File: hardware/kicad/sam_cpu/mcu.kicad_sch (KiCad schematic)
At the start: 38 parts, among them J19 USB-C (to Pi), J20 SWD, SW1 RESET, SW2 BOOTSEL, U4 RP2354B, U5 TPS3808G33, Y1 12MHz

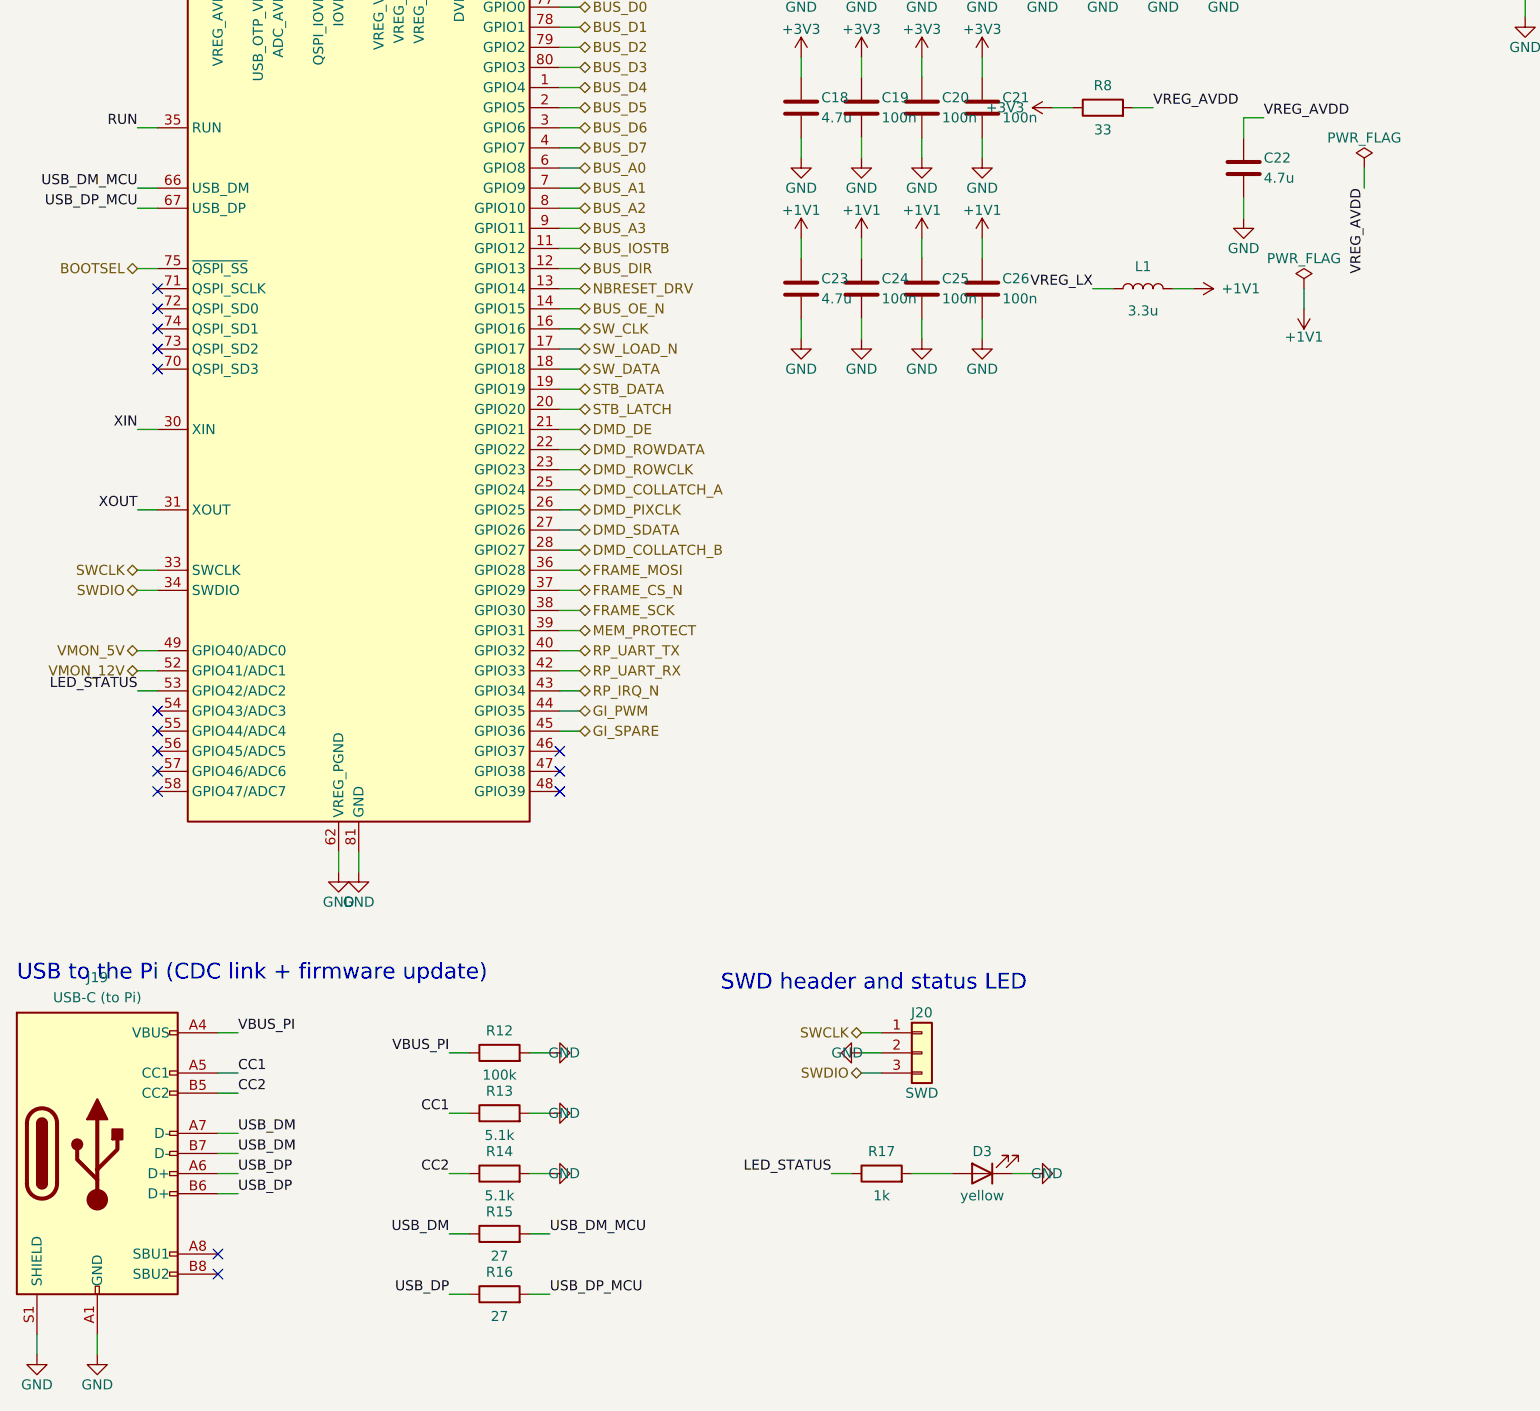
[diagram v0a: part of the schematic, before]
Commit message: Move the schematic to KiCad 10
Sheets regenerated from the KiCad 10.0.5 symbol library and saved in the
KiCad 10 file format with kicad-cli 10.0.6. ERC: 0 errors, 1 warning;
netlist unchanged (1266 pins, 299 nets).

Co-Authored-By: Claude Opus 5.5 (1M context) <noreply@anthropic.com>
Claude-Session: https://claude.ai/code/session_019DLTv1F2PjepjxqiUcAMKV
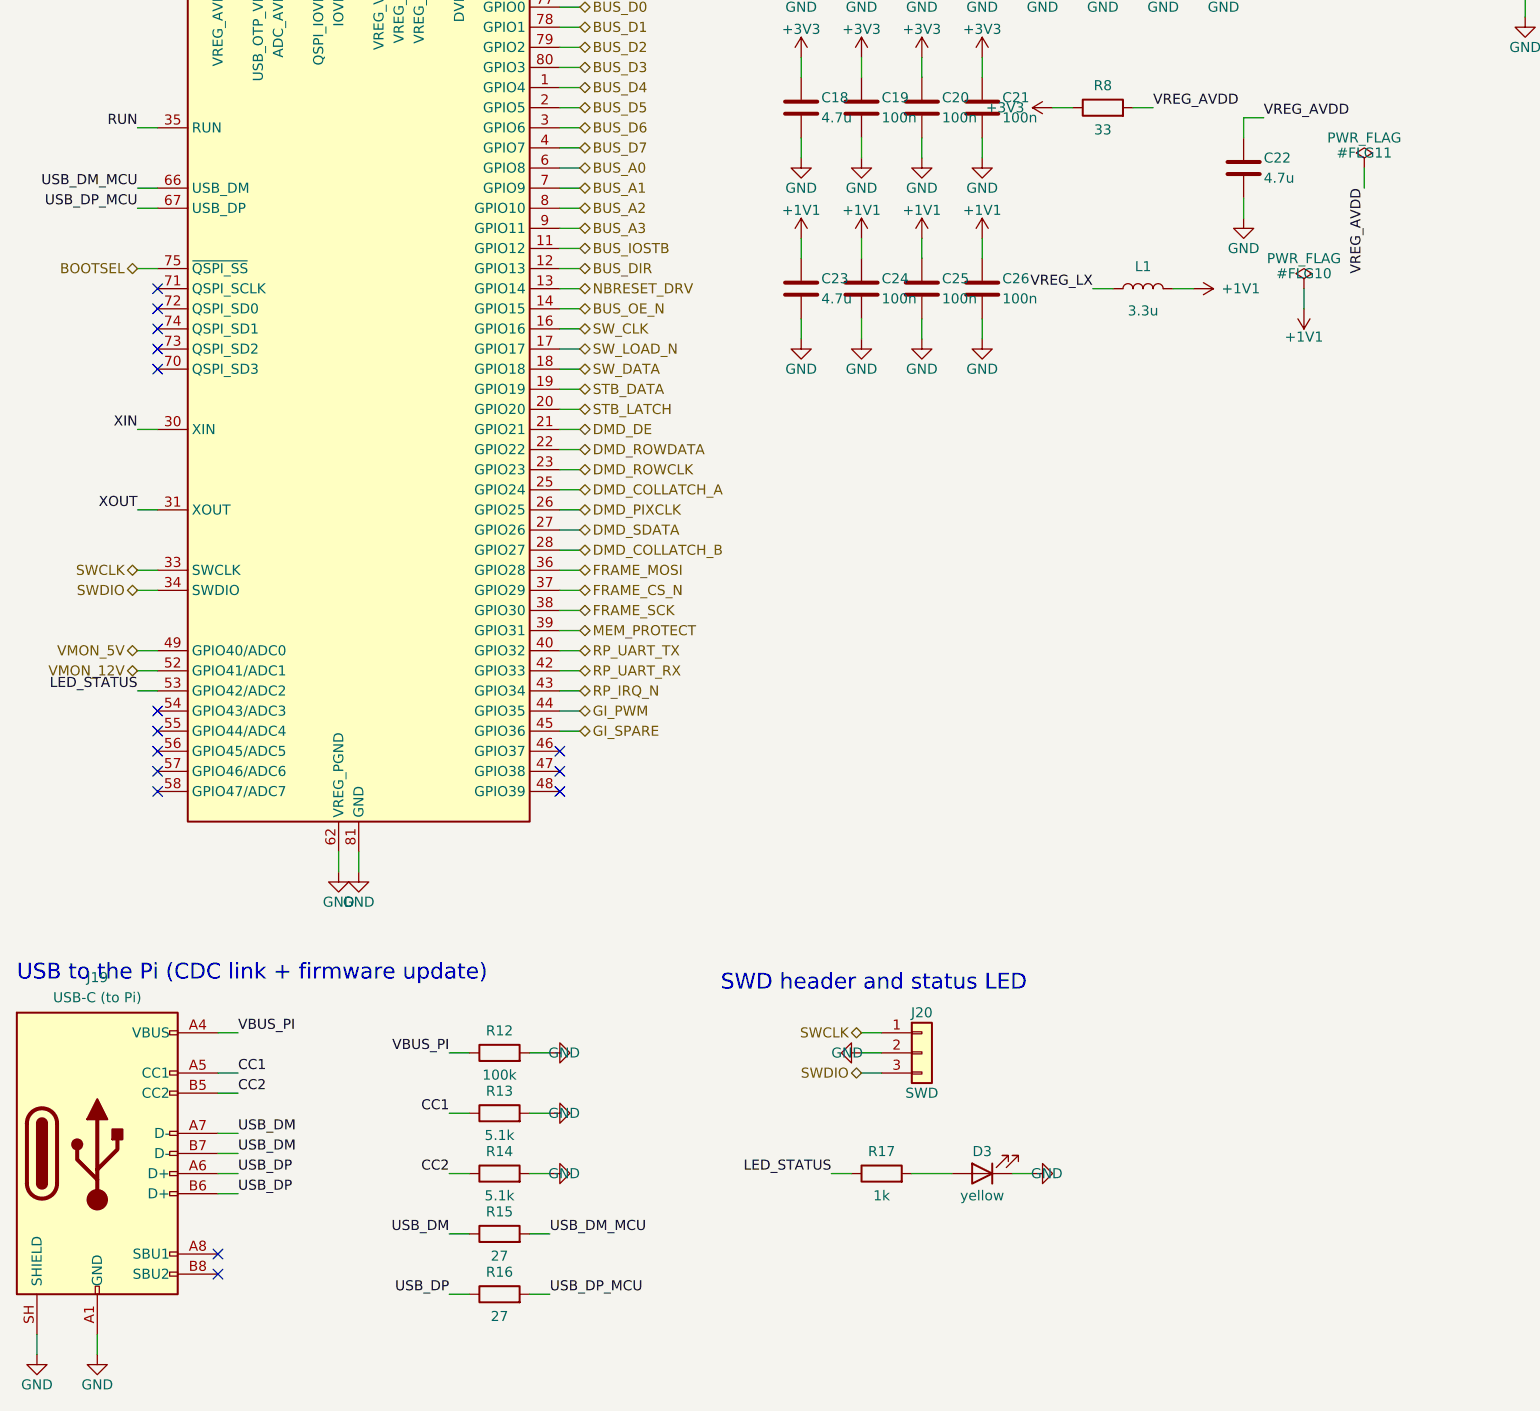
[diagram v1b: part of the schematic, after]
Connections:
- net GND: now also J19.SH (SHIELD); no longer J19.S1 (SHIELD)

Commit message: Redraw the schematic with wires (draft 0.2)
Every connection is now a wire, and each connector sits on the page of the
parts that drive or read it (Pi header with the RP2354B, J6/J12 with their
comparators and 74HC165, J1 with the 74HC595, J2/J3/J13 with their filters).
Signals between pages use global labels with page references. The Pi page is
merged into the MCU page; the Pi 4 sits on the 40-pin header J21.

ERC: 0 errors, 1 warning. Netlist check: 1266 pins, 299 nets, no differences.

Co-Authored-By: Claude Opus 5.5 (1M context) <noreply@anthropic.com>
Claude-Session: https://claude.ai/code/session_019DLTv1F2PjepjxqiUcAMKV
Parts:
- removed C10: 100n, Capacitor_SMD:C_0603_1608Metric, symbol Device:C
- added C29: 15p, Capacitor_SMD:C_0603_1608Metric, symbol Device:C
- added J21: Raspberry Pi 40-pin, Connector_PinSocket_2.54mm:PinSocket_2x20_P2.54mm_Vertical, symbol Connector:Raspberry_Pi_2_3
- added R18, R19: 33, Resistor_SMD:R_0603_1608Metric, symbol Device:R
- added R20, R21: 1k, Resistor_SMD:R_0603_1608Metric, symbol Device:R
- added R22: 10k, Resistor_SMD:R_0603_1608Metric, symbol Device:R
- C11, C12, C24: value 100n -> 4.7u; footprint Capacitor_SMD:C_0603_1608Metric -> Capacitor_SMD:C_0805_2012Metric
- C18, C22, C23: value 4.7u -> 100n; footprint Capacitor_SMD:C_0805_2012Metric -> Capacitor_SMD:C_0603_1608Metric
- C27: value 15p -> 100n
- R10: value 10k -> 100k
- R11: value 1k -> 5.1k
- R12: value 100k -> 5.1k
- R13, R14: value 5.1k -> 27
- R15, R16: value 27 -> 1k
- R9: value 1k -> 10k
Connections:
- net +1V1: now also C27.1; no longer C23.1
- net +3V3: now also C22.1, C23.1, R9.1, R22.1; no longer C11.1, R10.2
- net BOOTSEL: now also R15.2, R21.2; no longer R11.1
- net GND: now also R10.2, R11.2, C29.2, J21.14 (GND), J21.20 (GND), J21.25 (GND), J21.30 (GND), J21.34 (GND), J21.39 (GND), J21.6 (GND), J21.9 (GND); no longer R13.2, R14.2
- net MR_N: now also R20.2
- net SWCLK: now also J21.18 (GPIO24)
- net SWDIO: now also J21.22 (GPIO25)
- net at D3.2 (A): now also R17.1; no longer R17.2
- net BOOTSEL_BTN: no longer names the net of SW2.1
- net BOOTSEL_BTN: now also R15.1; no longer R11.2
- net CC1: no longer names the net of J19.A5 (CC1)
- net CC1: now also R11.1; no longer R13.1
- net CC2: no longer names the net of J19.B5 (CC2)
- net CC2: now also R12.1; no longer R14.1
- net FRAME_CS_N: no longer names the net of U4.37 (GPIO29)
- net FRAME_CS_N: now also J21.24 (~{CE0}/GPIO8)
- net FRAME_MOSI: no longer names the net of U4.36 (GPIO28)
- net FRAME_MOSI: now also J21.19 (MOSI0/GPIO10)
- net FRAME_SCK: no longer names the net of U4.38 (GPIO30)
- net FRAME_SCK: now also J21.23 (SCLK0/GPIO11)
- net LED_STATUS: no longer names the net of U4.53 (GPIO42/ADC2)
- net LED_STATUS: now also R17.2; no longer R17.1
- net RP_IRQ_N: no longer names the net of U4.43 (GPIO34)
- net RP_IRQ_N: now also J21.16 (GPIO23), R22.2
- net RP_UART_RX: no longer names the net of U4.42 (GPIO33)
- net RP_UART_RX: now also R18.2
- net RP_UART_TX: no longer names the net of U4.40 (GPIO32)
- net RP_UART_TX: now also R19.2
- net RUN: no longer names the net of U4.35 (RUN), U5.1 (~{RESET})
- net RUN: now also R9.2; no longer R10.1
- net USB_DM: no longer names the net of J19.A7 (D-), J19.B7 (D-)
- net USB_DM: now also R13.1; no longer R15.1
- net USB_DM_MCU: no longer names the net of U4.66 (USB_DM)
- net USB_DM_MCU: now also R13.2; no longer R15.2
- net USB_DP: no longer names the net of J19.A6 (D+), J19.B6 (D+)
- net USB_DP: now also R14.1; no longer R16.1
- net USB_DP_MCU: no longer names the net of R16.2
- net USB_DP_MCU: now also U4.31 (XOUT); no longer U4.67 (USB_DP)
- net VBUS_PI: no longer names the net of J19.A4 (VBUS), J19.A9 (VBUS), J19.B4 (VBUS), J19.B9 (VBUS)
- net VBUS_PI: now also R10.1; no longer R12.1
- net VREG_AVDD: no longer names the net of R8.2, U4.61 (VREG_AVDD)
- net VREG_AVDD: now also C11.1; no longer C22.1
- net VREG_LX: no longer names the net of L1.1, U4.63 (VREG_LX)
- net XIN: no longer names the net of U4.30 (XIN), Y1.1
- net XIN: now also C28.1; no longer C27.1
- removed net XOUT: R9.1, U4.31 (XOUT)
- removed net XTAL_OUT: C28.1, R9.2, Y1.3
- new net: J21.13 (GPIO27), R21.1
- new net: J21.1 (3V3), J21.17 (3V3)
- new net: J21.10 (GPIO15/RXD), R19.1
- new net: J21.15 (GPIO22), R20.1
- new net: J21.8 (GPIO14/TXD), R18.1
- new net: C29.1, R16.1, Y1.3
- new net: R14.2, U4.67 (USB_DP)
- new net +5V: J21.2 (5V), J21.4 (5V)
- new net I2S_BCK: J21.12 (GPIO18/PWM0)
- new net I2S_DIN: J21.40 (GPIO21/SCLK1)
- new net I2S_LRCK: J21.35 (GPIO19/MISO1)
- no-connect marks 16 -> 32
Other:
- note added: "GPIO map: ARCHITECTURE.md 9.2. PIO0 bus on GPIO0-15, PIO1 switch chain on GPIO16-20, PIO2 DMD on GPIO21-27, GPIO31 coin door memory protect. Core supply from the internal switching regulator: VREG_LX -> L1 -> DVDD (1.1 V); VREG_AVDD through 33 R / 4.7 uF. Check against the RP2350 hardware guide. Raspberry Pi 4 on the 40-pin header J21 (HDMI stays on the Pi). The Pi is powered from the board +5 V: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"
- note added: "Raspberry Pi 4 (40-pin header J21)"
- note removed: "12 MHz crystal"
- note removed: "Decoupling and core regulator"
- note removed: "GPIO map follows ARCHITECTURE.md 9.2: PIO0 bus on GPIO0-15, PIO1 switch chain on GPIO16-20, PIO2 DMD on GPIO21-27. GPIO31 reads the coin door memory protect input (J2 pin 10), which the doc does not list yet. Core supply from the internal switching regulator: VREG_LX -> L1 -> DVDD (1.1 V), VREG_AVDD through 33 R / 4.7 uF. Check these values against the RP2350 hardware design guide before layout."
- note removed: "RP2354B (2 MB flash in the package)"
- note removed: "Reset supervisor, RESET and BOOTSEL"
- note removed: "SWD header and status LED"
- note removed: "USB to the Pi (CDC link + firmware update)"
- title: RP2354B SAM IO controller -> RP2354B SAM IO controller and Raspberry Pi 4 header
- moved on the sheet: C11, C12, C13, C14, C15, C16, C17, C18, C19, C20, C21, C22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
